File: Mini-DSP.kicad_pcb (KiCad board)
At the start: 2 copper layers, 34 x 87.3 mm, 73 parts, among them J1 9V, J2 Barrel_Jack_MountingPin, J3 MOBO_Con, SW1 USB_BOOT, SW2 USB_BOOT, U1 CS4270, U2 AMS1117-3.3, U3 W25Q128JVS, U4 AMS1117-5.0, U5 APS1604M-3SQRx-SN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

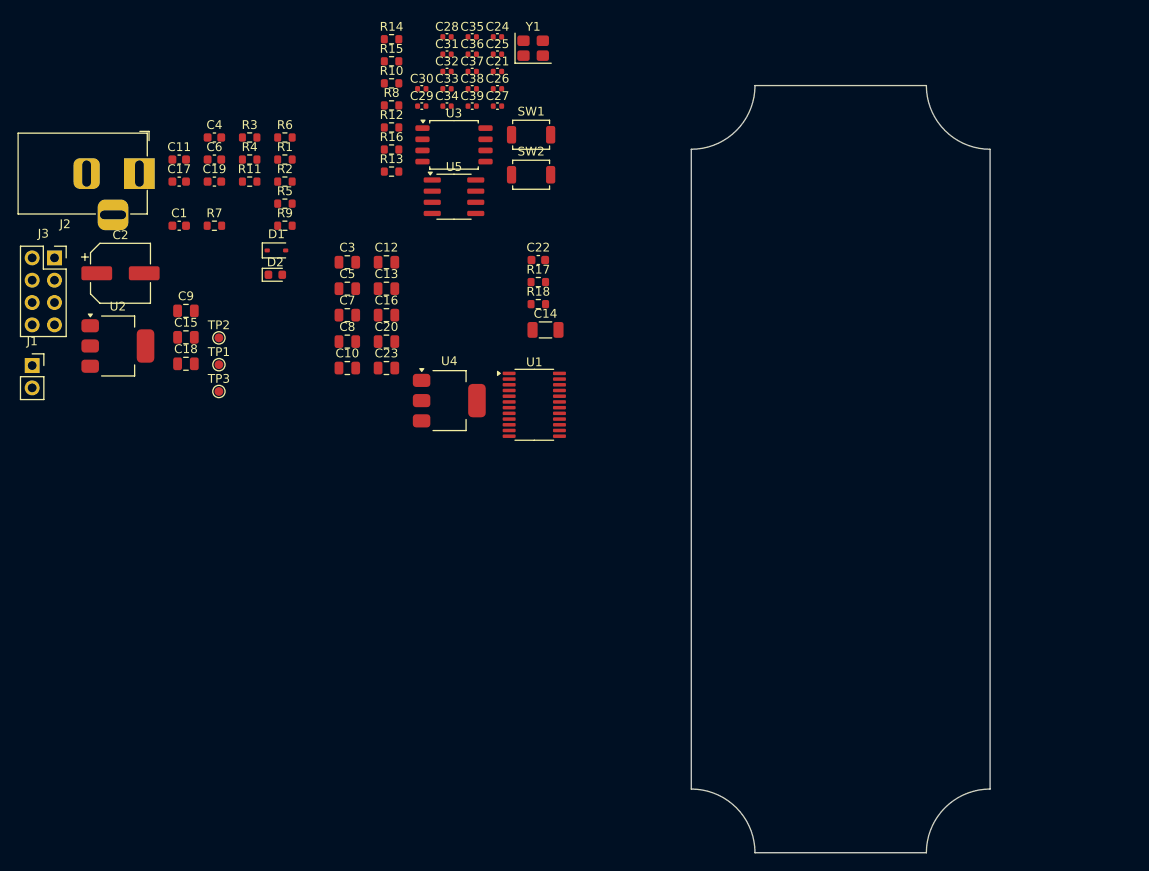
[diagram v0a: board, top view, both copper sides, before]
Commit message: update schematic and placement
- missing 3PDT part
- need to change CS4270 (EoL)
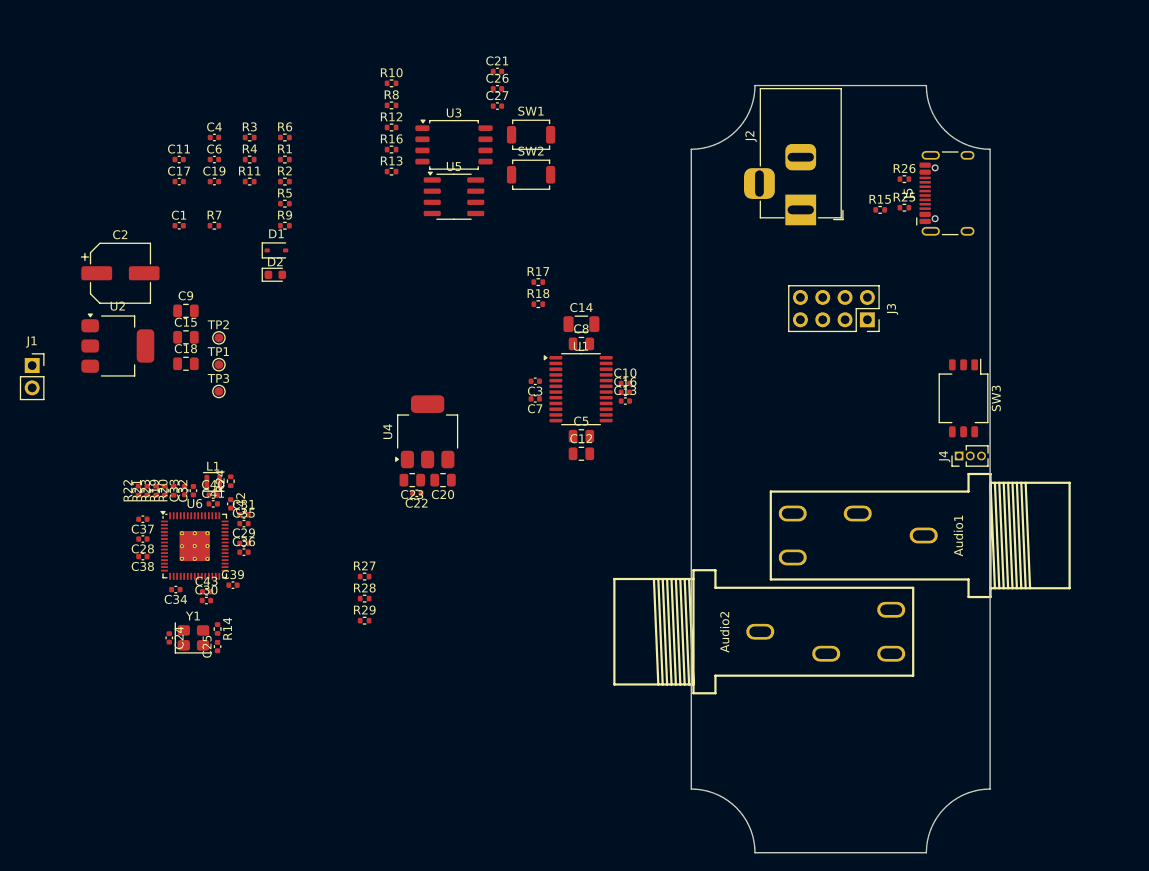
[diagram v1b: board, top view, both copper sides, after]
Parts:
- added Audio1: PJ-603A, easyeda2kicad:AUDIO-TH_PJ-603A, F.Cu at (191.5, 75.8)
- added Audio2: PJ-603A, easyeda2kicad:AUDIO-TH_PJ-603A, F.Cu at (187.8, 86.8)
- added C40: 4.7u, Capacitor_SMD:C_0402_1005Metric, F.Cu at (118.1, 71.2)
- added C41: 4.7u, Capacitor_SMD:C_0402_1005Metric, F.Cu at (118.1, 72.2)
- added C42: 4.7u, Capacitor_SMD:C_0402_1005Metric, F.Cu at (120.1, 72.2)
- added C43: 100n, Capacitor_SMD:C_0402_1005Metric, F.Cu at (117.3, 82.2)
- added J4: SWD, Connector_PinHeader_1.27mm:PinHeader_1x03_P1.27mm_Vertical, F.Cu at (203.0, 66.8)
- added J5: USB_C_Receptacle_USB2.0_16P, Connector_USB:USB_C_Receptacle_HCTL_HC-TYPE-C-16P-01A, F.Cu at (202.9, 36.9)
- added L1: AOTA-B201610S3R3-101-T, Inductor_SMD:L_Murata_DFE201610P, F.Cu at (118.1, 69.7)
- added R19: 33, Resistor_SMD:R_0402_1005Metric, F.Cu at (112.6, 70.7)
- added R20: 33, Resistor_SMD:R_0402_1005Metric, F.Cu at (113.6, 70.7)
- added R21: 33, Resistor_SMD:R_0402_1005Metric, F.Cu at (110.6, 70.7)
- added R22: 33, Resistor_SMD:R_0402_1005Metric, F.Cu at (109.6, 70.7)
- added R23: 33, Resistor_SMD:R_0402_1005Metric, F.Cu at (111.6, 70.7)
- added R24: 33, Resistor_SMD:R_0402_1005Metric, F.Cu at (120.1, 69.6)
- added R25: 5k1, Resistor_SMD:R_0402_1005Metric, F.Cu at (196.8, 38.5)
- added R26: 5k1, Resistor_SMD:R_0402_1005Metric, F.Cu at (196.8, 35.2)
- added R27: 10k, Resistor_SMD:R_0402_1005Metric, F.Cu at (135.3, 80.5)
- added R28: 10k, Resistor_SMD:R_0402_1005Metric, F.Cu at (135.3, 83.0)
- added R29: 10k, Resistor_SMD:R_0402_1005Metric, F.Cu at (135.3, 85.5)
- added SW3: MODE, Button_Switch_SMD:SW_DIP_SPSTx03_Slide_KingTek_DSHP03TS_W7.62mm_P1.27mm, F.Cu at (203.5, 60.2)
- added U6: RP2350A-QFN60, Package_DFN_QFN:QFN-60-1EP_7x7mm_P0.4mm_EP3.4x3.4mm_ThermalVias, F.Cu at (116.0, 77.0)
- C1, C11, C17, C19, C22, C4, C6: footprint Capacitor_SMD:C_0603_1608Metric -> Capacitor_SMD:C_0402_1005Metric
- C10, C13, C16, C3, C7: footprint Capacitor_SMD:C_0805_2012Metric -> Capacitor_SMD:C_0402_1005Metric
- R1, R10, R11, R12, R13, R14, R15, R16, R17, R18, R2, R3, R4, R5, R6, R7, R8, R9: footprint Resistor_SMD:R_0603_1608Metric -> Resistor_SMD:R_0402_1005Metric
- moved J3 92.8 mm to (192.5, 51.2), turned to -90 degrees
- moved C24 77.9 mm to (113.1, 87.5), turned to -90 degrees
- moved Y1 77.4 mm to (115.8, 87.5)
- moved J2 75.4 mm to (185.0, 38.8), turned to -90 degrees
- moved C25 74.6 mm to (118.6, 88.4), turned to 90 degrees
- moved R14 70.0 mm to (118.6, 86.4), turned to -90 degrees
- moved C28 66.8 mm to (110.1, 76.2), turned to 180 degrees
- moved C38 65.1 mm to (110.1, 78.2), turned to 180 degrees
- moved C37 63.2 mm to (110.1, 74.0), turned to 180 degrees
- moved C30 63.2 mm to (117.3, 83.2)
- moved C34 63.1 mm to (113.8, 82.0), turned to 180 degrees
- moved C36 62.3 mm to (121.6, 77.7)
- moved C35 61.2 mm to (121.6, 74.5)
- moved C39 60.9 mm to (120.3, 81.5)
- moved R15 58.1 mm to (194.0, 38.8)
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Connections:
- U1 pad 15: unconnected-(U1-AINA-Pad15) -> /IN
- U1 pad 21: unconnected-(U1-~{MUTEA}-Pad21) -> /~{MUTE_A}
- U1 pad 22: unconnected-(U1-OUTA-Pad22) -> /OUT
- U1 pad 24: unconnected-(U1-~{MUTEB}-Pad24) -> /~{MUTE_B}

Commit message: WIP
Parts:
- removed C22: 100n, Capacitor_SMD:C_0402_1005Metric
- removed C23: 10u, Capacitor_SMD:C_0805_2012Metric
- removed U1: CS4270, Package_SO:TSSOP-24_4.4x7.8mm_P0.65mm
- removed U4: AMS1117-5.0, Package_TO_SOT_SMD:SOT-223-3_TabPin2
- added C44: 100n, Capacitor_SMD:C_0402_1005Metric, F.Cu at (177.2, 64.0)
- added C45: 10u, Capacitor_SMD:C_0603_1608Metric, F.Cu at (176.5, 66.5)
- added C49: 100n, Capacitor_SMD:C_0402_1005Metric, F.Cu at (179.2, 64.0)
- added C50: 100n, Capacitor_SMD:C_0402_1005Metric, F.Cu at (180.2, 64.0)
- added D3: CTL1, LED_SMD:LED_0603_1608Metric, F.Cu at (204.8, 35.0)
- added R30: 330, Resistor_SMD:R_0402_1005Metric, F.Cu at (202.2, 35.0)
- added U7: ES8388, Package_DFN_QFN:QFN-28-1EP_4x4mm_P0.45mm_EP2.6x2.6mm, F.Cu at (179.3, 60.0)
- C10, C13, C16: value 100n -> 10u; footprint Capacitor_SMD:C_0402_1005Metric -> Capacitor_SMD:C_0603_1608Metric
- C12: value 10u -> 1u
- C14: value 47u -> 10u; footprint Capacitor_SMD:C_1206_3216Metric -> Capacitor_SMD:C_0603_1608Metric
- C15, C18, C9: footprint Capacitor_SMD:C_0805_2012Metric -> Capacitor_SMD:C_0603_1608Metric
- C20: value 10u -> 100n; footprint Capacitor_SMD:C_0805_2012Metric -> Capacitor_SMD:C_0402_1005Metric
- C5: value 1u -> 10u; footprint Capacitor_SMD:C_0805_2012Metric -> Capacitor_SMD:C_0603_1608Metric
- C7: value 100n -> 1u; footprint Capacitor_SMD:C_0402_1005Metric -> Capacitor_SMD:C_0805_2012Metric
- C8: value 1u -> 100n; footprint Capacitor_SMD:C_0805_2012Metric -> Capacitor_SMD:C_0402_1005Metric
- U6: value RP2350A-QFN60 -> RP2354A-QFN60
- moved C24 97.3 mm to (204.7, 54.5), turned to 0 degrees
- moved R8 95.9 mm to (199.2, 101.0), turned to 90 degrees
- moved Y1 95.7 mm to (204.7, 51.8), turned to 90 degrees
- moved C25 95.6 mm to (205.7, 49.0), turned to 180 degrees
- moved C34 93.4 mm to (201.8, 50.5), turned to -90 degrees
- moved R14 92.9 mm to (203.7, 49.0), turned to 0 degrees
- moved C30 92.8 mm to (202.9, 47.3), turned to 90 degrees
- moved C43 91.5 mm to (201.9, 47.3), turned to 90 degrees
- moved C38 91.2 mm to (198.1, 54.3), turned to -90 degrees
- moved J1 91.1 mm to (184.0, 28.0), turned to 90 degrees
- moved C39 89.2 mm to (201.3, 44.0), turned to 90 degrees
- moved U2 88.8 mm to (194.5, 37.8), turned to 180 degrees
- moved C28 88.7 mm to (196.1, 54.3), turned to -90 degrees
- moved C2 88.1 mm to (194.2, 30.5)
- moved C17 86.8 mm to (201.0, 39.2), turned to -90 degrees
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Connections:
- C10 pad 1: +5V -> +3V3
- C12 pad 1: /VCOM -> Net-(U7-LOUT1)
- C12 pad 2: GND -> /OUT
- C13 pad 1: /VCOM -> Net-(U7-VREF)
- C14 pad 1: /FILT -> Net-(U7-ADCVREF)
- C16 pad 1: /FILT -> Net-(U7-VMID)
- C20 pad 1: +9V -> +3V3
- C7 pad 1: +3V3 -> Net-(U7-LIN1)
- C7 pad 2: GND -> /IN
- C8 pad 1: +5V -> +3V3
- R12 pad 1: unconnected-(R12-Pad1) -> /PSRAM_SS
- U6 pad 13: unconnected-(U6-GPIO9-Pad13) -> /I^{2}S_SDOUT
- U6 pad 14: unconnected-(U6-GPIO10-Pad14) -> /I^{2}S_LRCK
- U6 pad 15: unconnected-(U6-GPIO11-Pad15) -> /I^{2}S_SCLK
- U6 pad 16: unconnected-(U6-GPIO12-Pad16) -> /I^{2}S_MCLK
- U6 pad 32: unconnected-(U6-GPIO20-Pad32) -> Net-(U6-GPIO20)
